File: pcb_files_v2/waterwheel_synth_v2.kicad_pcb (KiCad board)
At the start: 2 copper layers, 171.7 x 171.7 mm, 192 parts, among them J1 Drum_SW_BD, J10 LEDS_volca, J11 Drum_Returns, J12 volc audio in/out. button trig, J13 RELAY out, J14 panel pots, J2 Drum_SW_SD, J3 Drum_sw_HH, J4 12x binary outs, 2x ins, J5 LED_drums, J6 Drum_sw_TT, J7 Volca_steps, J8 LED_binary, J9 power and clock, K1 G5Q-1, Q1 2N3904, Q10 2N3904, Q11 2N3904, Q12 2N3904, Q13 2N3904, Q14 2N3904, Q15 2N3904, Q16 2N3904, Q17 2N3904, Q18 2N3904, Q19 2N3904, Q2 2N3904, Q20 2N3904, Q21 2N3904, Q22 2N3904, Q23 2N3904, Q24 2N3904, Q25 2N3904, Q3 2N3904, Q4 2N3904, Q5 2N3904, Q6 2N3904, Q7 2N3904, Q8 2N3904, Q9 2N3904, U1 4017, U10 Teensy3.2, U2 4069, U4 4017, U5 4040, U6 4081, U7 4017, U8 555(NEW_layout), U9 4066

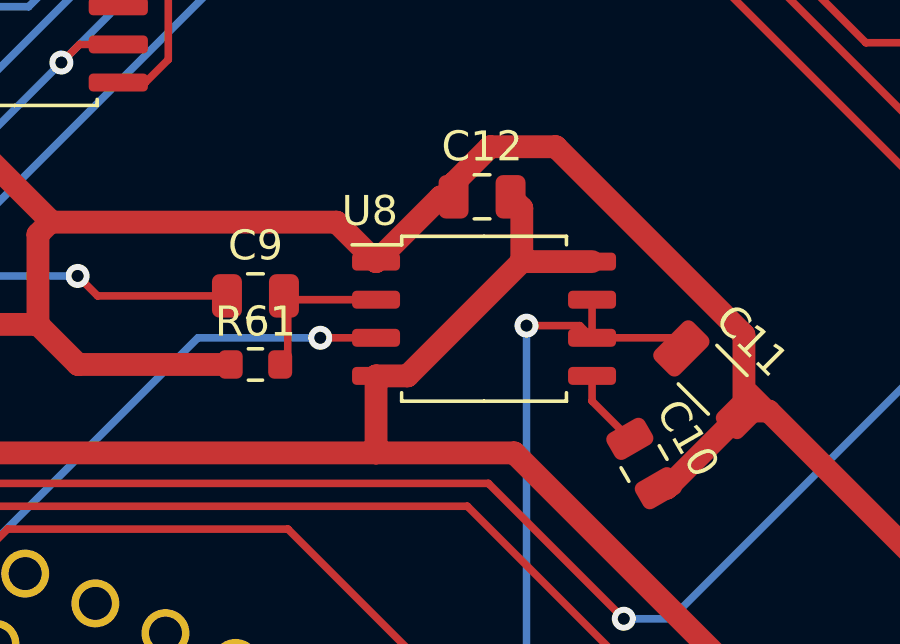
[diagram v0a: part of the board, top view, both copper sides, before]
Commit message: updated 555 footprint, it was too big
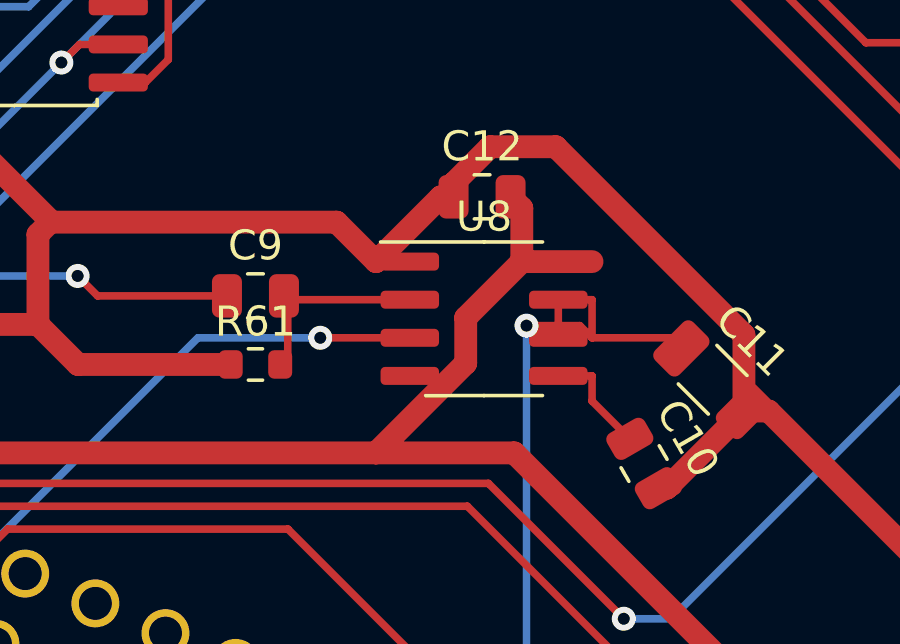
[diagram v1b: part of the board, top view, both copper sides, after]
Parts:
- U8: footprint Package_SO:SOIC-8_5.275x5.275mm_P1.27mm -> Package_SO:SOIC-8_3.9x4.9mm_P1.27mm
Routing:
- net hold_pot: track 47.5 -> 49.9 mm
- net ambient_trigger_to_teensy: track 35.8 -> 37.0 mm
- net Net-(C9-Pad2): track 5.39 -> 6.51 mm
- net Net-(C10-Pad1): track 2.62 -> 3.74 mm
- net +5V: track 452.2 -> 451.6 mm
